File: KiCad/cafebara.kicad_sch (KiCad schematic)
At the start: 60 parts, among them J1 Micro_SD_Card_Det2, J2 USB_C_Receptacle_USB2.0_14P, J3 PROG, J4 Conn_01x19_MountingPin, J6 EDID, Q1 NMOS, SW1 SW_Push, U3 ATtiny1616-M, U4 M24C02-RMC, U5 BQ25895RTW

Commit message: Begin change to new battery charge IC
TODO:
- complete transition
- add battery protection
- add fuel gauge?
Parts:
- removed C11: 22uF, Capacitor_SMD:C_0805_2012Metric, symbol Device:C_Small
- added C11: 100uF, Capacitor_Tantalum_SMD:CP_EIA-3216-10_Kemet-I, symbol Device:C_Polarized_Small
- added C21, C22: 33nF, Capacitor_SMD:C_0402_1005Metric, symbol Device:C_Small
- added Q2, Q3, Q4, Q5, Q7, Q8: NMOS, symbol Simulation_SPICE:NMOS
- added Q6: PMOS, symbol Simulation_SPICE:PMOS
- added R10: 5m, Resistor_SMD:R_0805_2012Metric, symbol Device:R_Small
- added TP12: BATT-, TestPoint:TestPoint_Plated_Hole_D2.0mm, symbol Connector:TestPoint
- added U6: BQ297xy, Package_SON:WSON-6_1.5x1.5mm_P0.5mm, symbol Battery_Management:BQ297xy
- added U7: BQ27441-G1, Package_SON:Texas_S-PDSO-N12, symbol Battery_Management:BQ27441-G1
- C1: footprint Capacitor_SMD:C_0603_1608Metric -> Capacitor_SMD:C_0805_2012Metric
- C13: value 10uF -> 47nF; footprint Capacitor_SMD:C_0603_1608Metric -> Capacitor_SMD:C_0402_1005Metric
- C14: value 4.7uF -> 10nF
- C16: value 10uF -> 10nF; footprint Capacitor_SMD:C_0603_1608Metric -> Capacitor_SMD:C_0402_1005Metric
- C20: value 10uF -> 1nF; footprint Capacitor_SMD:C_0603_1608Metric -> Capacitor_SMD:C_0402_1005Metric
- C8: value 22uF -> 1uF
- L1: value 3.3uH -> 4.7uH; Digikey https://www.digikey.com.au/en/products/detail/tai-tech-adva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 -> (none)
- R6: value 260 -> 2.2
- R7: value 5.23k -> 4.99
- R8: value 30.1k -> 4.99
- TP5: value BATT -> BATT+
- U5: value BQ25895RTW -> BQ25730RSN; footprint Package_DFN_QFN:Texas_RTW_WQFN-24-1EP_4x4mm_P0.5mm_EP2.7x2.7mm_ThermalVias -> Package_DFN_QFN:Texas_RSN_WQFN-32-1EP_4x4mm_P0.4mm_EP2.8x2.8mm_ThermalVias; Digikey (none) -> https://www.digikey.com.au/en/products/detail/texas-instrum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
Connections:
- net GND: now also C8.2, U5.27 (PGND), U5.33 (PGND), C11.2, C21.2, C22.2, Q3.3 (S), Q4.3 (S), Q8.3 (S); no longer BT1.2 (-), C13.2, C14.1, C8.1, R6.1, R8.1, U5.17 (PGND), U5.18 (PGND), U5.25 (PGND), U5.9 (~{CE})
- net SCL: now also U5.13 (SCL); no longer U5.5 (SCL)
- net SDA: now also U5.12 (SDA); no longer U5.6 (SDA)
- net VBUS: now also R6.2, R7.2, C11.1, R10.2
- net VCC: now also U5.22 (VSYS), Q5.1 (D), Q6.3 (S); no longer L1.2, U5.15 (SYS), U5.16 (SYS)
- net at U5.10 (PSYS): no longer R6.2
- net SW1: now reaches C12.1, L1.1
- net SW1: now also U5.32 (SW1), Q2.3 (S), Q3.1 (D); no longer U5.19 (SW), U5.20 (SW)
- net ACN: now reaches U5.2 (ACN)
- net ACN: now also C14.2, R8.1, C22.1
- net at C12.2: now also U5.30 (BTST1); no longer U5.21 (BTST)
- net SW2: now reaches U5.23 (SW2)
- net SW2: now also C13.1, L1.2, Q4.1 (D), Q5.3 (S); no longer C8.2
- net HIDRV2: now reaches U5.24 (HIDRV2)
- net HIDRV2: now also Q5.2 (G)
- net ACP: now reaches U5.3 (ACP)
- net ACP: now also C14.1, R7.1, C21.1
- removed net BATT: BT1.1 (+), C13.1, C16.1, C20.1, TP5.1, U5.13 (BAT), U5.14 (BAT)
- net BQ_STAT: no longer names the net of U5.4 (CHRG_OK)
- net ~{BQ_INT}: no longer names the net of U5.7 (VDDA)
- net ~{BQ_INT}: no longer U3.15 (PC0)
- new net: C16.1, C20.1, Q2.1 (D), R10.1, R8.2
- new net: C13.2, U5.25 (BTST2)
- new net: Q7.1 (D), Q8.1 (D)
- new net: Q7.2 (G), U6.3 (Dout)
- new net: C8.1, R6.1
- new net: Q8.2 (G), U6.2 (Cout)
- new net BATT+: TP5.1
- new net BATT-: Q7.3 (S), TP12.1, U6.4 (VSS)
- new net HIDRV1: Q2.2 (G), U5.31 (HIDRV1)
- new net LODRV1: Q3.2 (G), U5.29 (LODRV1)
- new net LODRV2: Q4.2 (G), U5.26 (LODRV2)
- new net SRN: U5.19 (SRN)
- new net SRP: U5.20 (SRP)
- new net ~{BATDRV}: Q6.2 (G), U5.21 (~{BATDRV})
- now unconnected: U5.11 (TS)
- no-connect marks 17 -> 13
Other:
- note added: "TODO: EDIT TO BQ27426, maybe"
- moved on the sheet: BT1, C10, C15, C17, C18, C19, C9, L1, R6, TP5, TP8, TP9

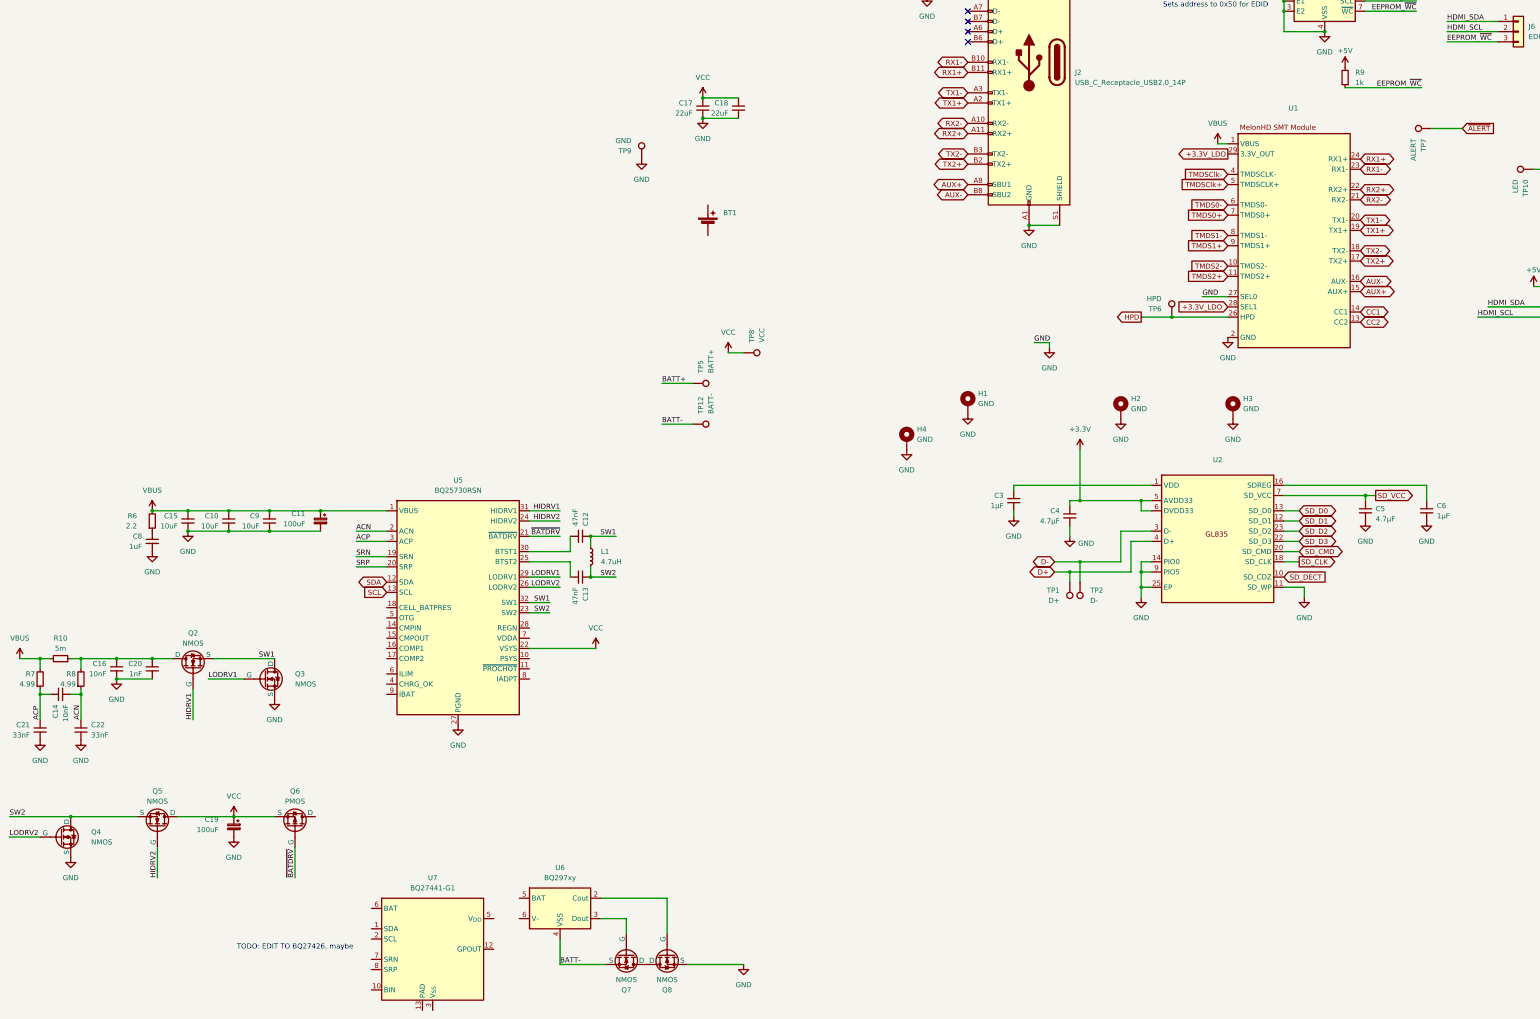
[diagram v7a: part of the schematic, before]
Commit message: Began migration to 2S configuration
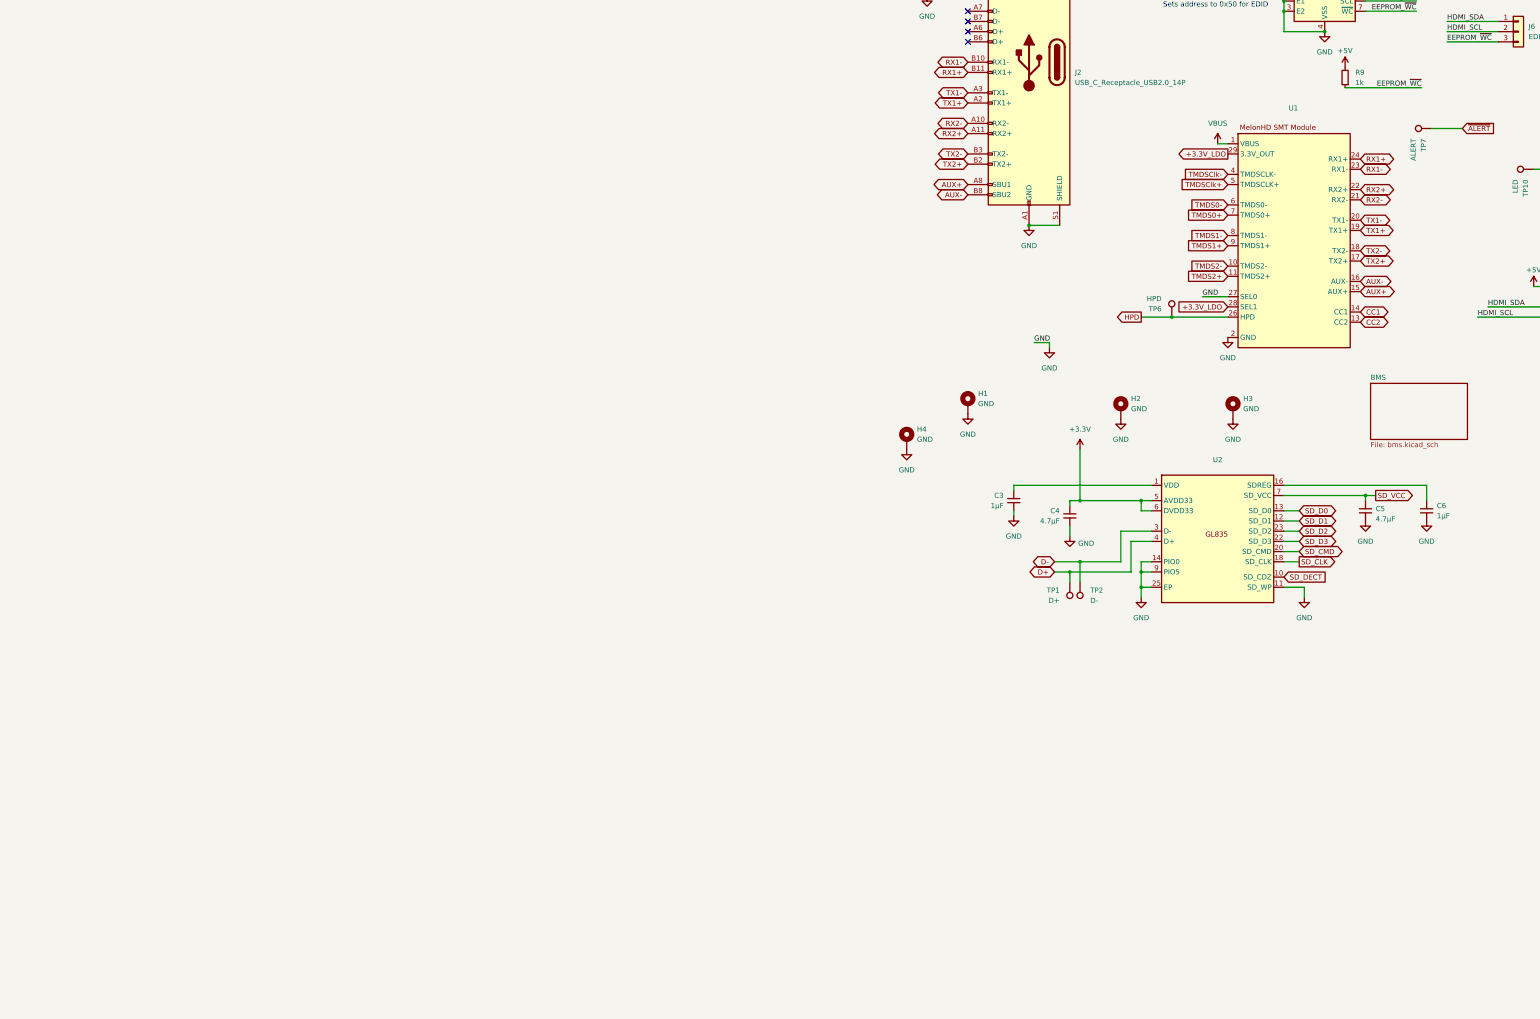
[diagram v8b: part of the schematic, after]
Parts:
- removed BT1: Battery_Cell, symbol Device:Battery_Cell
- removed C10, C15, C9: 10uF, Capacitor_SMD:C_0603_1608Metric, symbol Device:C_Small
- removed C11, C19: 100uF, Capacitor_Tantalum_SMD:CP_EIA-3216-10_Kemet-I, symbol Device:C_Polarized_Small
- removed C12, C13: 47nF, Capacitor_SMD:C_0402_1005Metric, symbol Device:C_Small
- removed C14, C16: 10nF, Capacitor_SMD:C_0402_1005Metric, symbol Device:C_Small
- removed C17, C18: 22uF, Capacitor_SMD:C_0402_1005Metric, symbol Device:C_Small
- removed C20: 1nF, Capacitor_SMD:C_0402_1005Metric, symbol Device:C_Small
- removed C21, C22: 33nF, Capacitor_SMD:C_0402_1005Metric, symbol Device:C_Small
- removed C8: 1uF, Capacitor_SMD:C_0402_1005Metric, symbol Device:C_Small
- removed L1: 4.7uH, Inductor_SMD:L_APV_APH0420, symbol Device:L_Small
- removed Q2, Q3, Q4, Q5, Q7, Q8: NMOS, symbol Simulation_SPICE:NMOS
- removed Q6: PMOS, symbol Simulation_SPICE:PMOS
- removed R10: 5m, Resistor_SMD:R_0805_2012Metric, symbol Device:R_Small
- removed R6: 2.2, Resistor_SMD:R_0402_1005Metric, symbol Device:R_Small
- removed R7, R8: 4.99, Resistor_SMD:R_0402_1005Metric, symbol Device:R_Small
- removed TP12: BATT-, TestPoint:TestPoint_Plated_Hole_D2.0mm, symbol Connector:TestPoint
- removed TP5: BATT+, TestPoint:TestPoint_Plated_Hole_D2.0mm, symbol Connector:TestPoint
- removed TP8: VCC, TestPoint:TestPoint_Plated_Hole_D2.0mm, symbol Connector:TestPoint
- removed TP9: GND, TestPoint:TestPoint_Plated_Hole_D2.0mm, symbol Connector:TestPoint
- removed U5: BQ25730RSN, Package_DFN_QFN:Texas_RSN_WQFN-32-1EP_4x4mm_P0.4mm_EP2.8x2.8mm_ThermalVias, symbol Battery_Management:BQ25895RTW
- removed U6: BQ297xy, Package_SON:WSON-6_1.5x1.5mm_P0.5mm, symbol Battery_Management:BQ297xy
- removed U7: BQ27441-G1, Package_SON:Texas_S-PDSO-N12, symbol Battery_Management:BQ27441-G1
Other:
- added sheet BMS (bms.kicad_sch)
- note removed: "TODO: EDIT TO BQ27426, maybe"
